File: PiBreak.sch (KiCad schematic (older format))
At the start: 5 parts, among them P1 RASPBERRY_PI_P1, P2 CONN_17, P3 CONN_8, P4 CONN_8, P5 CONN_8

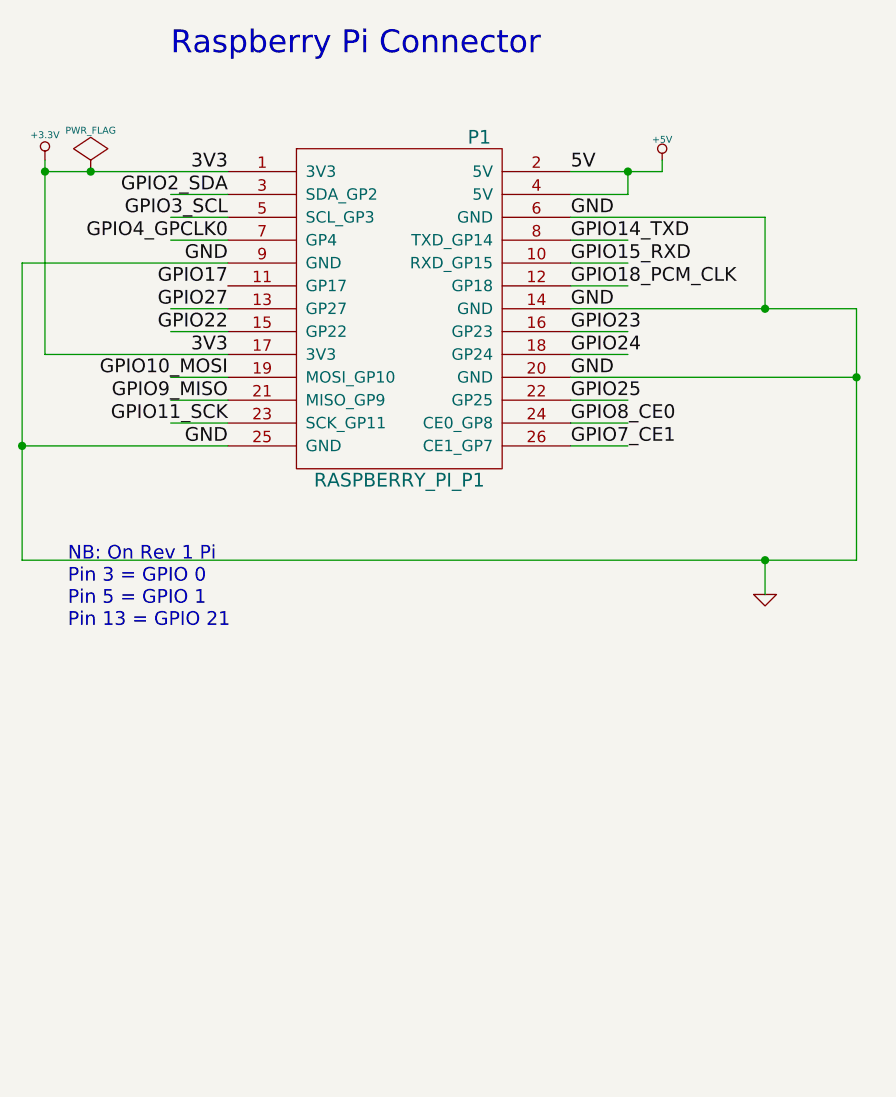
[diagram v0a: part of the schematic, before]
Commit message: Add 4x2 header for P5 pins
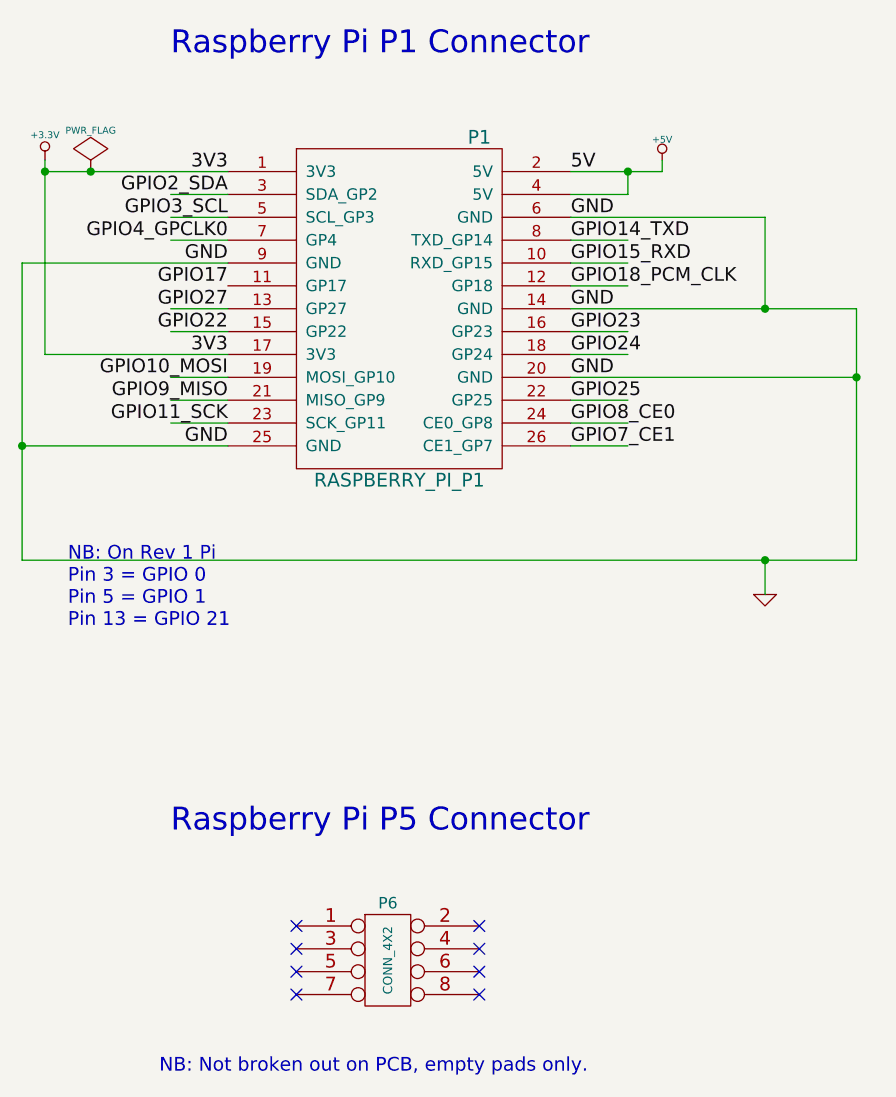
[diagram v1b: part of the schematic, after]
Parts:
- added P6: CONN_4X2, ~, symbol CONN_4X2
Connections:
- no-connect marks 0 -> 8
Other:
- note added: "NB: Not broken out on PCB, empty pads only."
- note added: "Raspberry Pi P1 Connector"
- note added: "Raspberry Pi P5 Connector"
- note removed: "Raspberry Pi Connector"
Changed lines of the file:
@@
 Sheet 1 1
 Title ""
-Date "27 nov 2013"
+Date "14 apr 2014"
 Rev ""
 Comp ""
@@
 $EndDescr
 Text Notes 1700 1800 0    100  ~ 0
-Raspberry Pi Connector
+Raspberry Pi P1 Connector
 Text Label 1950 2300 2    60   ~ 0
 3V3
@@
 GPIO7_CE1
 $Comp
-L GND #PWR3
+L GND #PWR01
 U 1 1 52089C00
 P 4300 4150
-F 0 "#PWR3" H 4300 4150 30  0001 C CNN
+F 0 "#PWR01" H 4300 4150 30  0001 C CNN
 F 1 "GND" H 4300 4080 30  0001 C CNN
 F 2 "" H 4300 4150 60  0000 C CNN
@@
 $EndComp
 $Comp
-L +5V #PWR2
+L +5V #PWR02
 U 1 1 5208AA34
 P 3850 2250
-F 0 "#PWR2" H 3850 2340 20  0001 C CNN
+F 0 "#PWR02" H 3850 2340 20  0001 C CNN
 F 1 "+5V" H 3850 2340 30  0000 C CNN
 F 2 "" H 3850 2250 60  0000 C CNN
@@
 Connection ~ 1150 2300
 $Comp
-L +3.3V #PWR1
+L +3.3V #PWR03
 U 1 1 520A14AA
 P 1150 2250
-F 0 "#PWR1" H 1150 2210 30  0001 C CNN
+F 0 "#PWR03" H 1150 2210 30  0001 C CNN
 F 1 "+3.3V" H 1150 2360 30  0000 C CNN
 F 2 "" H 1150 2250 60  0000 C CNN
@@
 $EndComp
 $Comp
-L PWR_FLAG #FLG1
+L PWR_FLAG #FLG04
 U 1 1 520A14B9
 P 1350 2300
-F 0 "#FLG1" H 1350 2395 30  0001 C CNN
+F 0 "#FLG04" H 1350 2395 30  0001 C CNN
 F 1 "PWR_FLAG" H 1350 2480 30  0000 C CNN
 F 2 "" H 1350 2300 60  0000 C CNN
@@
 Connection ~ 8350 2350
 $Comp
-L +5V #PWR4
+L +5V #PWR05
 U 1 1 5296803C
 P 8350 2250
-F 0 "#PWR4" H 8350 2340 20  0001 C CNN
+F 0 "#PWR05" H 8350 2340 20  0001 C CNN
 F 1 "+5V" H 8350 2340 30  0000 C CNN
 F 2 "" H 8350 2250 60  0000 C CNN
@@
 $EndComp
 $Comp
-L +3.3V #PWR5
+L +3.3V #PWR06
 U 1 1 529680F0
 P 8950 2250
-F 0 "#PWR5" H 8950 2210 30  0001 C CNN
+F 0 "#PWR06" H 8950 2210 30  0001 C CNN
 F 1 "+3.3V" H 8950 2360 30  0000 C CNN
 F 2 "" H 8950 2250 60  0000 C CNN
@@
 $EndComp
 $Comp
-L GND #PWR6
+L GND #PWR07
 U 1 1 529681D3
 P 9550 3200
-F 0 "#PWR6" H 9550 3200 30  0001 C CNN
+F 0 "#PWR07" H 9550 3200 30  0001 C CNN
 F 1 "GND" H 9550 3130 30  0001 C CNN
 F 2 "" H 9550 3200 60  0000 C CNN
@@
 Text Notes 8550 1800 0    100  ~ 0
 Power Breakouts
+$Comp
+L CONN_4X2 P6
+U 1 1 534B8765
+P 2650 5750
+F 0 "P6" H 2650 6000 50  0000 C CNN
+F 1 "CONN_4X2" V 2650 5750 40  0000 C CNN
+F 2 "~" H 2650 5750 60  0000 C CNN
+F 3 "~" H 2650 5750 60  0000 C CNN
+	1    2650 5750
+	1    0    0    -1
+$EndComp
+Text Notes 1700 5200 0    100  ~ 0
+Raspberry Pi P5 Connector
+NoConn ~ 2250 5600
+NoConn ~ 2250 5700
+NoConn ~ 2250 5800
+NoConn ~ 2250 5900
+NoConn ~ 3050 5600
+NoConn ~ 3050 5700
+NoConn ~ 3050 5800
+NoConn ~ 3050 5900
+Text Notes 1650 6250 0    60   ~ 0
+NB: Not broken out on PCB, empty pads only.
 $EndSCHEMATC
